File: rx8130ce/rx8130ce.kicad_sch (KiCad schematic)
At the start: 11 parts, among them J3 Conn_01x05, J4 Conn_01x05, U1 RX8130CE

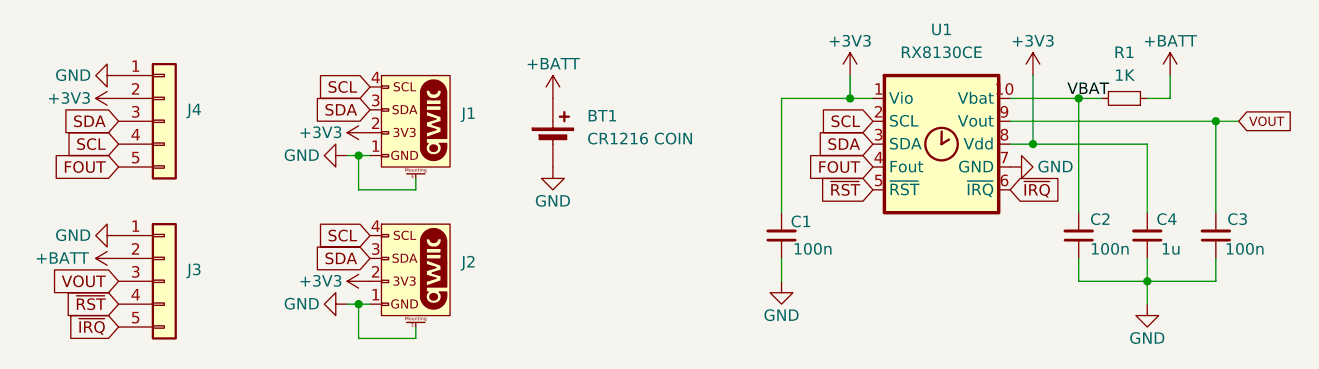
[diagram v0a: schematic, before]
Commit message: bump to KiCAD 10
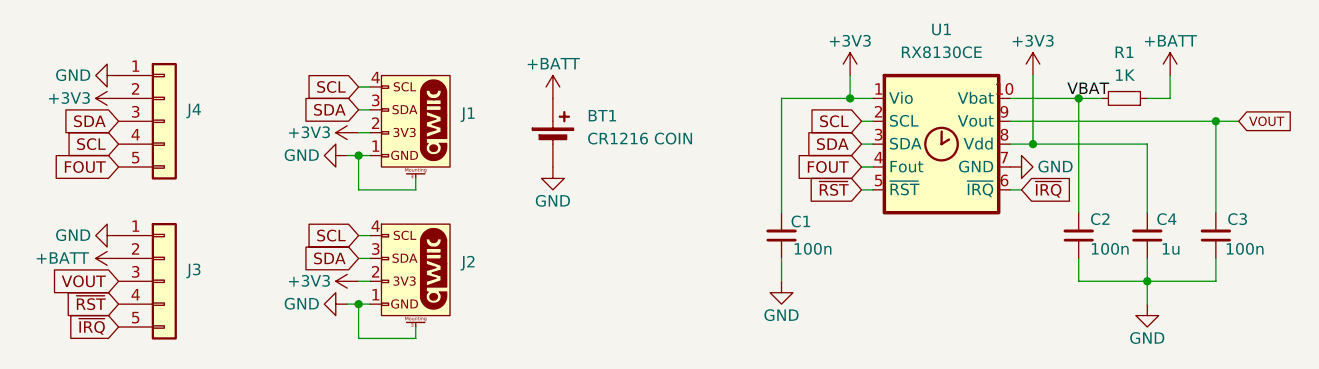
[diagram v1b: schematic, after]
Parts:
- J1, J2: value ~ -> (none)
